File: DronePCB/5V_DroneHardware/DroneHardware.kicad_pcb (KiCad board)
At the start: 6 copper layers, 36.1 x 36 mm, 41 parts, among them J201 USB_B_Micro, J202 BATTERY, J203 SWD_CONN, SW1 SW_SPDT, U1 STM32F405RGT6, U303 MPU-6000, Y1 16MHz

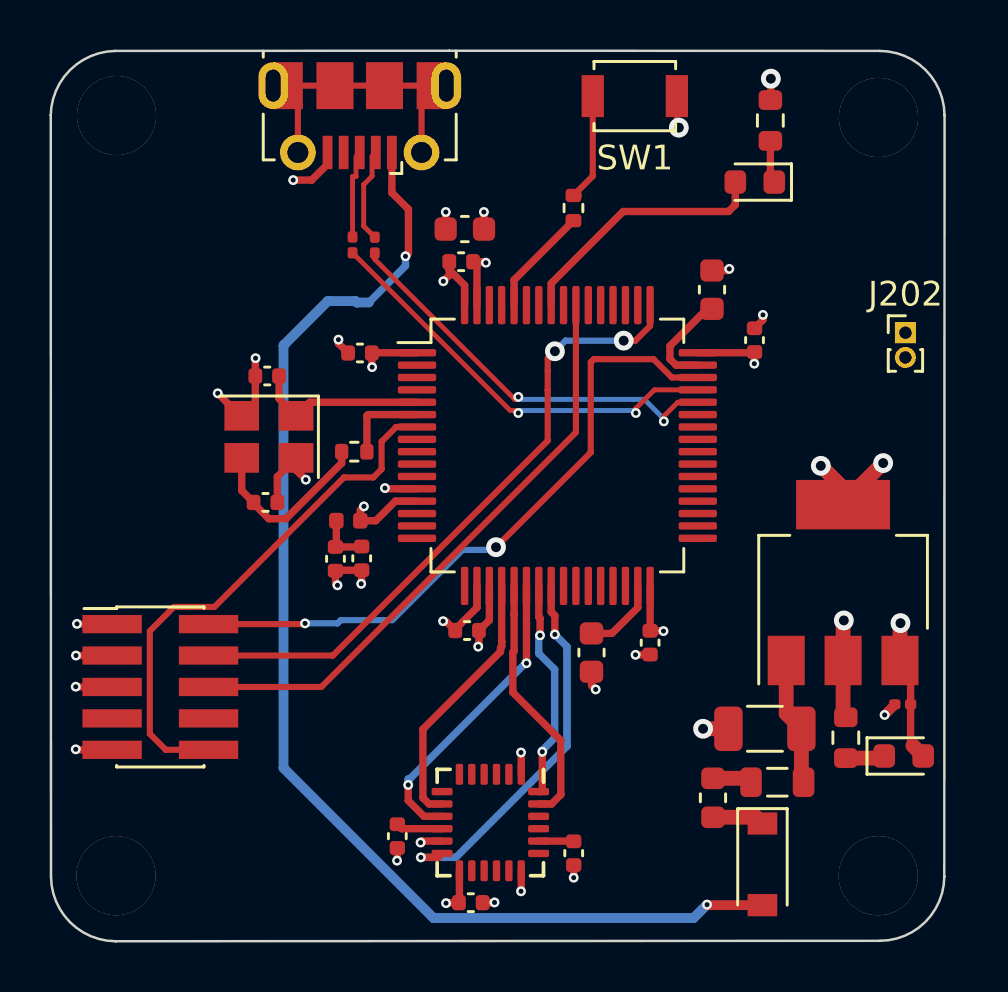
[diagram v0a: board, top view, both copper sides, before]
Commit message: Collegamento di dei segnali PWM dei motori
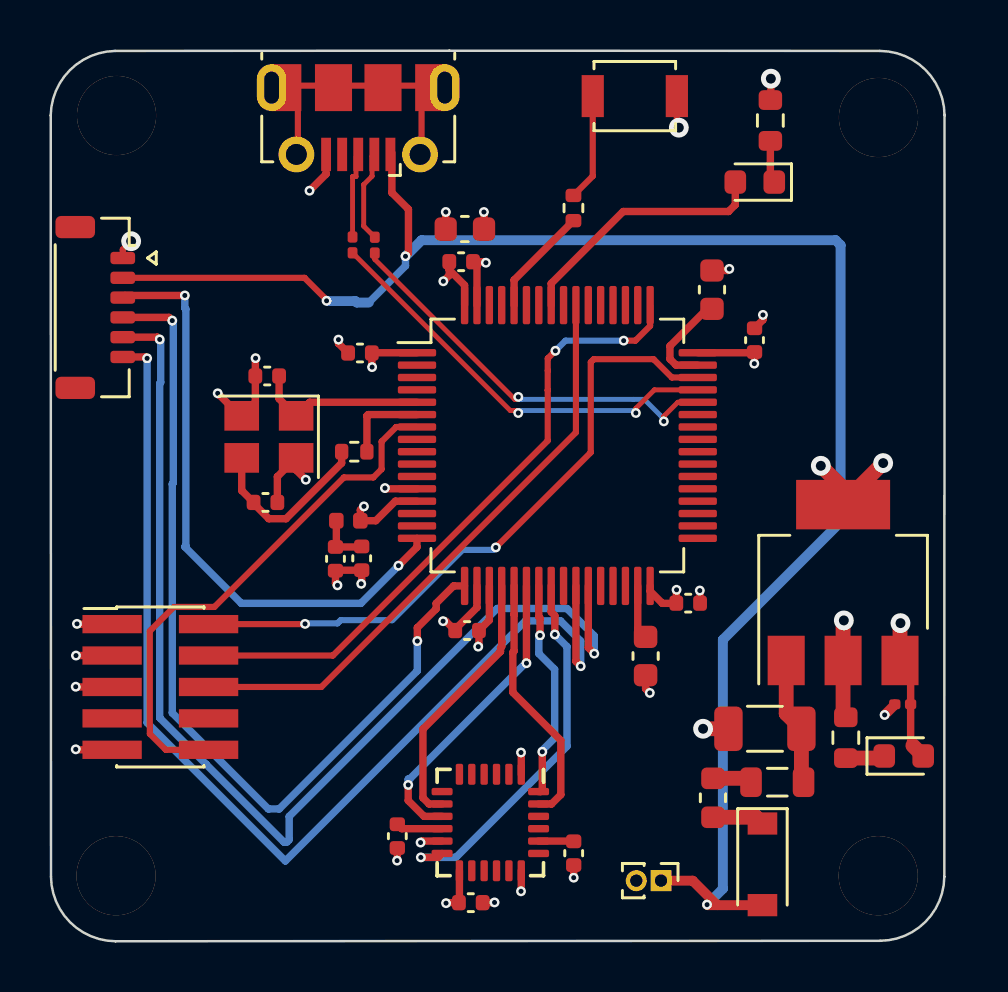
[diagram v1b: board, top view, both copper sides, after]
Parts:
- added J204: Conn_01x06_Male, Connector_Hirose:Hirose_DF52-6S-0.8H_1x06-1MP_P0.80mm_Horizontal, F.Cu at (129.7, 93.5)
- moved J202 24.3 mm to (152.6, 116.6), turned to -90 degrees
- moved C4 2.22 mm to (153.7, 105.4), turned to 0 degrees
- moved C1 2.19 mm to (152.0, 107.5)
- moved J201 0.10 mm to (140.4, 85.8)
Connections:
- J202 pad 1: +12V -> +5V
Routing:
- net PWM2: track 0.00 -> 45.0 mm, vias 0 -> 2
- net PWM1: track 0.00 -> 44.3 mm, vias 0 -> 2
- net PWM3: track 0.00 -> 36.3 mm, vias 0 -> 2
- net PWM4: track 0.00 -> 24.4 mm, vias 0 -> 2
- net +5V: track 50.4 -> 69.1 mm, vias 2 -> 3
- net Net-(C1-Pad1): track 3.18 -> 2.19 mm
- net GND: track 41.4 -> 41.8 mm, vias 30 -> 31
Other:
- copper layers 6 -> 4

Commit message: Aggiunta di USART per RC
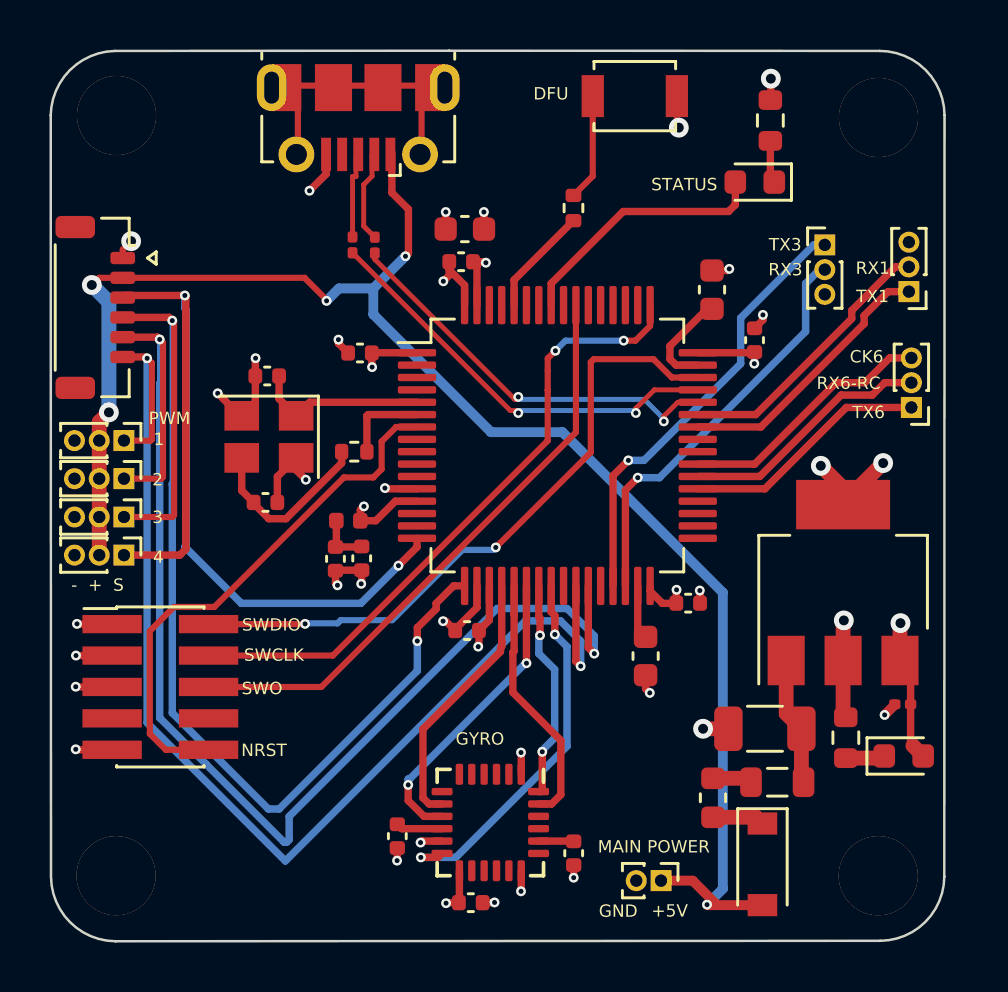
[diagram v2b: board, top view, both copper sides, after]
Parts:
- added G***: LOGO, Footprints:LogoVespin20x17p5, B.Cu at (156.2, 106.8)
- added J205: Conn_01x03_Female, Connector_PinHeader_1.00mm:PinHeader_1x03_P1.00mm_Vertical, F.Cu at (130.9, 98.8)
- added J206: Conn_01x03_Female, Connector_PinHeader_1.00mm:PinHeader_1x03_P1.00mm_Vertical, F.Cu at (130.9, 100.4)
- added J207: Conn_01x03_Female, Connector_PinHeader_1.00mm:PinHeader_1x03_P1.00mm_Vertical, F.Cu at (130.9, 101.9)
- added J208: Conn_01x03_Female, Connector_PinHeader_1.00mm:PinHeader_1x03_P1.00mm_Vertical, F.Cu at (130.9, 103.5)
- added J209: Conn_01x03_Female, Connector_PinHeader_1.00mm:PinHeader_1x03_P1.00mm_Vertical, F.Cu at (162.7, 97.5)
- added J210: Conn_01x03_Female, Connector_PinHeader_1.00mm:PinHeader_1x03_P1.00mm_Vertical, F.Cu at (162.6, 92.8)
- added J211: Conn_01x03_Female, Connector_PinHeader_1.00mm:PinHeader_1x03_P1.00mm_Vertical, F.Cu at (159.2, 90.9)
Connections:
- U1 pad 29: unconnected-(U1-Pad29) -> USART3_TX
- U1 pad 30: unconnected-(U1-Pad30) -> USART3_RX
- U1 pad 37: unconnected-(U1-Pad37) -> USART6_TX
- U1 pad 38: unconnected-(U1-Pad38) -> USART6_RX
- U1 pad 39: unconnected-(U1-Pad39) -> USART6_CK
- U1 pad 42: unconnected-(U1-Pad42) -> USART1_TX
- U1 pad 43: unconnected-(U1-Pad43) -> USART1_RX
- U1 pad 61: PPM -> unconnected-(U1-Pad61)
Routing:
- net USART3_TX: track 0.00 -> 18.0 mm, vias 0 -> 1
- net USART3_RX: track 0.00 -> 16.8 mm, vias 0 -> 1
- net PWM4: track 24.4 -> 37.2 mm
- net USART1_RX: track 0.00 -> 11.2 mm
- net USART1_TX: track 0.00 -> 11.0 mm
- net USART6_CK: track 0.00 -> 10.4 mm
- net USART6_RX: track 0.00 -> 10.2 mm
- net USART6_TX: track 0.00 -> 10.00 mm
- net PWM3: track 36.3 -> 46.2 mm
- net PWM2: track 45.0 -> 52.2 mm
- net PWM1: track 44.3 -> 48.8 mm
- net +5V: track 69.1 -> 67.5 mm, vias 3 -> 5
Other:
- board text added: "+5V"
- board text added: "- + S"
- board text added: "1"
- board text added: "2"
- board text added: "3"
- board text added: "4"
- board text added: "Author: Giovanni Rasera Link: https://github.com/GiovanniRaseraF"
- board text added: "CK6"
- board text added: "DFU"
- board text added: "GND"
- board text added: "GYRO"
- board text added: "MAIN POWER"
- board text added: "NRST"
- board text added: "PWM"
- board text added: "RX1"
- board text added: "RX3"
- board text added: "RX6-RC"
- board text added: "STATUS"
- board text added: "SWCLK"
- board text added: "SWDIO"
- board text added: "SWO"
- board text added: "TX1"
- board text added: "TX3"
- board text added: "TX6"
- board text added: "Ver: 1.0 - 4 PWM - URT 1 3 6 - Gyro - 5V to 3.3 - No 12V batt !!"

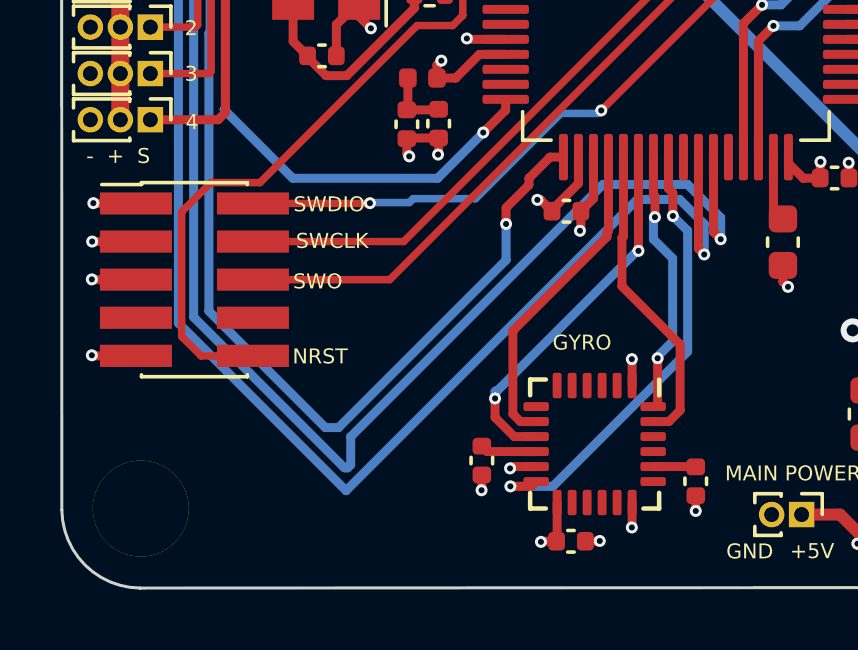
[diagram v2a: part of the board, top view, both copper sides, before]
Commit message: Pulizia delle tracce
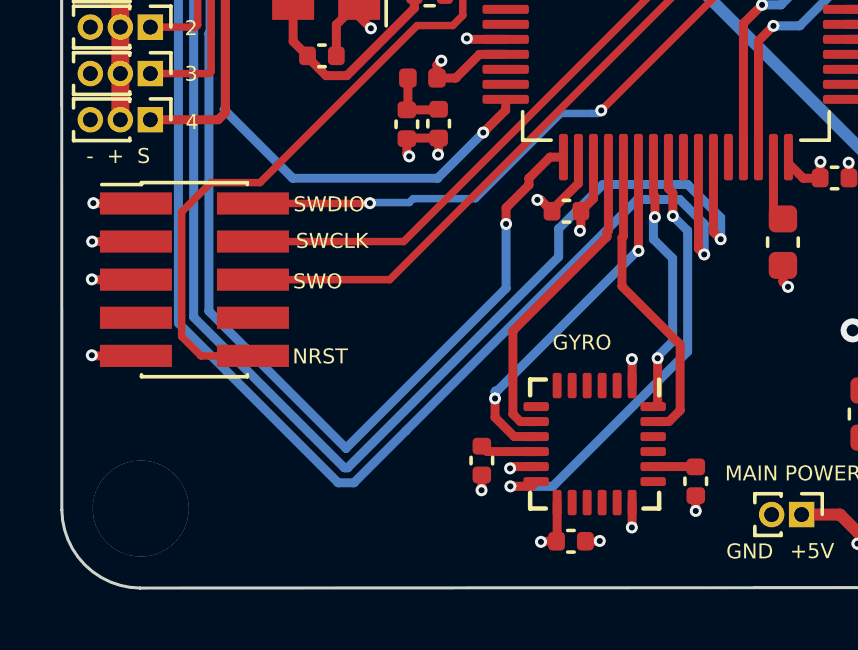
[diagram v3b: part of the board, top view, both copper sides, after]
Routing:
- net PWM3: track 46.2 -> 47.3 mm
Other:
- board text added: "Ver: 1.0 - 4 PWM - URT 1 3 6 - Gyro - 5V to 3.3V - No 12V batt !!"
- board text removed: "Ver: 1.0 - 4 PWM - URT 1 3 6 - Gyro - 5V to 3.3 - No 12V batt !!"
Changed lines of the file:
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@@
   (gr_line (start 130.528672 83.078504) (end 144.04 83.07) (layer "Edge.Cuts") (width 0.1))
   (gr_arc (start 127.928478 85.68) (mid 128.704288 83.855227) (end 130.528672 83.078504) (layer "Edge.Cuts") (width 0.1))
-  (gr_text "Ver: 1.0\n- 4 PWM\n- URT 1 3 6\n- Gyro\n- 5V to 3.3 \n- No 12V batt !!" (at 154.1 91.64) (layer "B.SilkS")
+  (gr_text "Ver: 1.0\n- 4 PWM\n- URT 1 3 6\n- Gyro\n- 5V to 3.3V\n- No 12V batt !!" (at 154.1 91.64) (layer "B.SilkS")
     (effects (font (size 1 1) (thickness 0.15)) (justify left mirror))
   )
@@
   (via (at 142.748 106.934) (size 0.4) (drill 0.2) (layers "F.Cu" "B.Cu") (net 35))
   (via (at 132.842 93.98) (size 0.4) (drill 0.2) (layers "F.Cu" "B.Cu") (net 35))
-  (segment (start 136.723428 113.720572) (end 137.165873 113.720572) (width 0.3) (layer "B.Cu") (net 35))
-  (segment (start 142.748 108.138445) (end 142.748 106.934) (width 0.3) (layer "B.Cu") (net 35))
-  (segment (start 132.842 109.839144) (end 136.723428 113.720572) (width 0.3) (layer "B.Cu") (net 35))
-  (segment (start 137.165873 113.720572) (end 142.748 108.138445) (width 0.3) (layer "B.Cu") (net 35))
+  (segment (start 132.883511 94.021511) (end 132.883511 100.542489) (width 0.3) (layer "B.Cu") (net 35))
+  (segment (start 137.411428 114.408572) (end 137.416572 114.408572) (width 0.3) (layer "B.Cu") (net 35))
+  (segment (start 132.842 100.584) (end 132.842 109.839144) (width 0.3) (layer "B.Cu") (net 35))
+  (segment (start 132.842 109.839144) (end 137.411428 114.408572) (width 0.3) (layer "B.Cu") (net 35))
+  (segment (start 142.748 109.077144) (end 142.748 106.934) (width 0.3) (layer "B.Cu") (net 35))
+  (segment (start 137.416572 114.408572) (end 142.748 109.077144) (width 0.3) (layer "B.Cu") (net 35))
+  (segment (start 132.842 93.98) (end 132.883511 94.021511) (width 0.3) (layer "B.Cu") (net 35))
   (segment (start 132.883511 100.542489) (end 132.842 100.584) (width 0.3) (layer "B.Cu") (net 35))
-  (segment (start 132.883511 94.021511) (end 132.883511 100.542489) (width 0.3) (layer "B.Cu") (net 35))
-  (segment (start 132.842 93.98) (end 132.883511 94.021511) (width 0.3) (layer "B.Cu") (net 35))
-  (segment (start 132.842 100.584) (end 132.842 109.839144) (width 0.3) (layer "B.Cu") (net 35))
   (segment (start 156.8 100.78) (end 160.09 97.49) (width 0.3) (layer "F.Cu") (net 37))
   (segment (start 154.085 100.78) (end 156.8 100.78) (width 0.3) (layer "F.Cu") (net 37))
@@
   (via (at 149.352 107.95) (size 0.4) (drill 0.2) (layers "F.Cu" "B.Cu") (net 56))
   (segment (start 149.352 106.934039) (end 149.352 107.95) (width 0.3) (layer "B.Cu") (net 56))
-  (segment (start 137.414 115.824) (end 147.120557 106.117443) (width 0.3) (layer "B.Cu") (net 56))
   (segment (start 131.826 95.504) (end 131.826 110.236) (width 0.3) (layer "B.Cu") (net 56))
+  (segment (start 139.414 113.824) (end 147.120557 106.117443) (width 0.3) (layer "B.Cu") (net 56))
   (segment (start 147.120557 106.117443) (end 148.535404 106.117443) (width 0.3) (layer "B.Cu") (net 56))
+  (segment (start 137.67648 115.561519) (end 139.414 113.824) (width 0.3) (layer "B.Cu") (net 56))
   (segment (start 148.535404 106.117443) (end 149.352 106.934039) (width 0.3) (layer "B.Cu") (net 56))
-  (segment (start 131.826 110.236) (end 137.414 115.824) (width 0.3) (layer "B.Cu") (net 56))
+  (segment (start 131.826 110.236) (end 137.151519 115.561519) (width 0.3) (layer "B.Cu") (net 56))
+  (segment (start 137.151519 115.561519) (end 137.67648 115.561519) (width 0.3) (layer "B.Cu") (net 56))
   (segment (start 143.590596 115.679404) (end 143.75 115.52) (width 0.3) (layer "F.Cu") (net 57))
   (segment (start 142.890908 115.679404) (end 143.590596 115.679404) (width 0.3) (layer "F.Cu") (net 57))
@@
   (via (at 132.334 94.742) (size 0.4) (drill 0.2) (layers "F.Cu" "B.Cu") (net 70))
   (segment (start 132.375511 96.478489) (end 132.334 96.52) (width 0.3) (layer "B.Cu") (net 70))
-  (segment (start 137.469572 115.062) (end 137.568786 114.962786) (width 0.3) (layer "B.Cu") (net 70))
+  (segment (start 132.334 110.037572) (end 137.358428 115.062) (width 0.3) (layer "B.Cu") (net 70))
+  (segment (start 132.334 96.52) (end 132.334 110.037572) (width 0.3) (layer "B.Cu") (net 70))
+  (segment (start 144.500786 107.092087) (end 145.97495 105.617923) (width 0.3) (layer "B.Cu") (net 70))
+  (segment (start 132.375511 94.783511) (end 132.375511 96.478489) (width 0.3) (layer "B.Cu") (net 70))
   (segment (start 137.358428 115.062) (end 137.469572 115.062) (width 0.3) (layer "B.Cu") (net 70))
+  (segment (start 137.469572 115.062) (end 144.500786 108.030786) (width 0.3) (layer "B.Cu") (net 70))
+  (segment (start 148.797923 105.617923) (end 149.9015 106.7215) (width 0.3) (layer "B.Cu") (net 70))
+  (segment (start 132.334 94.742) (end 132.375511 94.783511) (width 0.3) (layer "B.Cu") (net 70))
   (segment (start 145.97495 105.617923) (end 148.797923 105.617923) (width 0.3) (layer "B.Cu") (net 70))
-  (segment (start 132.334 96.52) (end 132.334 110.037572) (width 0.3) (layer "B.Cu") (net 70))
-  (segment (start 148.797923 105.617923) (end 149.9015 106.7215) (width 0.3) (layer "B.Cu") (net 70))
+  (segment (start 144.500786 108.030786) (end 144.500786 107.092087) (width 0.3) (layer "B.Cu") (net 70))
   (segment (start 149.9015 106.7215) (end 149.9015 107.442) (width 0.3) (layer "B.Cu") (net 70))
-  (segment (start 132.334 110.037572) (end 134.211214 111.914786) (width 0.3) (layer "B.Cu") (net 70))
-  (segment (start 132.334 94.742) (end 132.375511 94.783511) (width 0.3) (layer "B.Cu") (net 70))
-  (segment (start 137.568786 114.024087) (end 145.97495 105.617923) (width 0.3) (layer "B.Cu") (net 70))
-  (segment (start 132.375511 94.783511) (end 132.375511 96.478489) (width 0.3) (layer "B.Cu") (net 70))
-  (segment (start 137.568786 114.962786) (end 137.568786 114.024087) (width 0.3) (layer "B.Cu") (net 70))
-  (segment (start 134.211214 111.914786) (end 137.358428 115.062) (width 0.3) (layer "B.Cu") (net 70))
   (segment (start 151.16 100.83) (end 151.66 100.33) (width 0.3) (layer "F.Cu") (net 72))
   (segment (start 151.16 104.705) (end 151.16 100.83) (width 0.3) (layer "F.Cu") (net 72))
